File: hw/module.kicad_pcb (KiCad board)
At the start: 2 copper layers, 30 x 30 mm, 35 parts, among them Q1 MUN 2211, U1 CFPS-39, U2 CFPS-39, U3 74LVC1G125, U4 74 LVC 1G3157GW,125, U5 MAX919, U6 STM32L010F4P6, U7 BAS70-7-F, U8 SS39ET, U9 LM 61BIM3

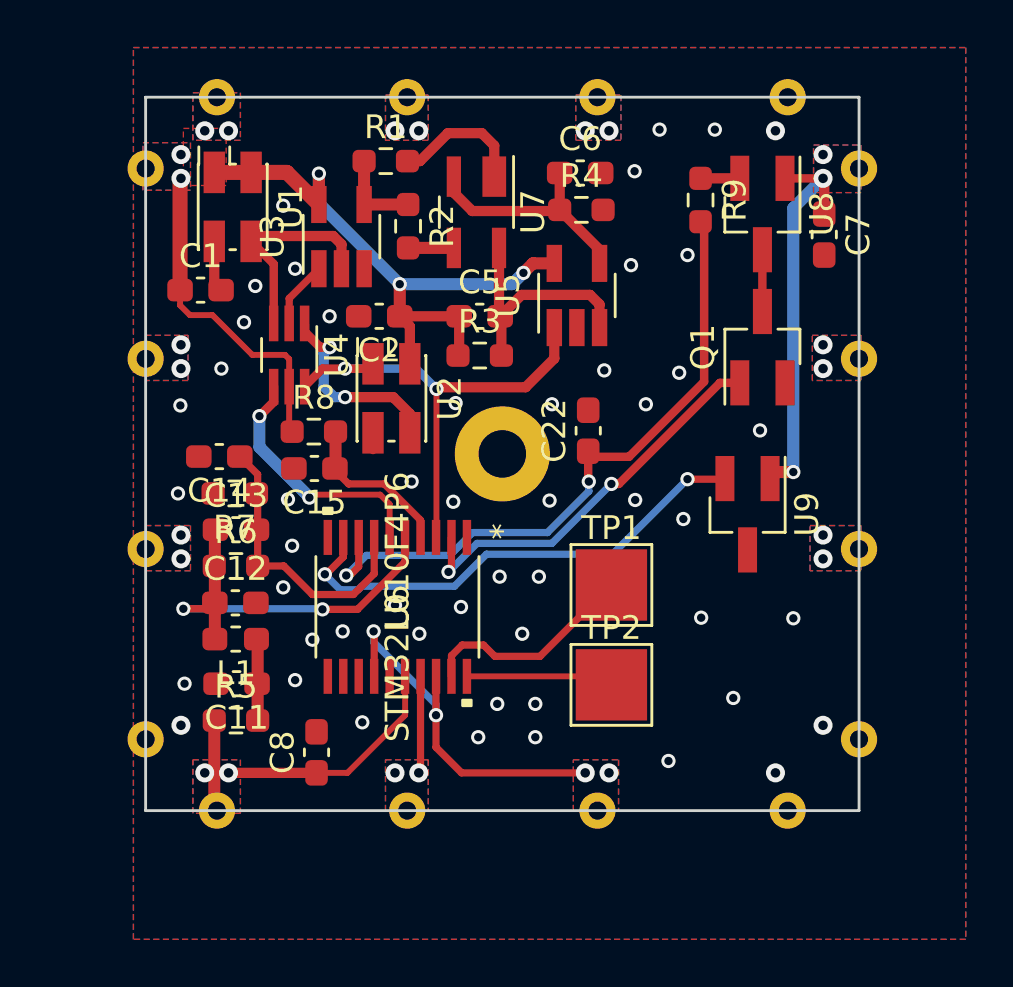
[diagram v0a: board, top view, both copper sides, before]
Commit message: added bom
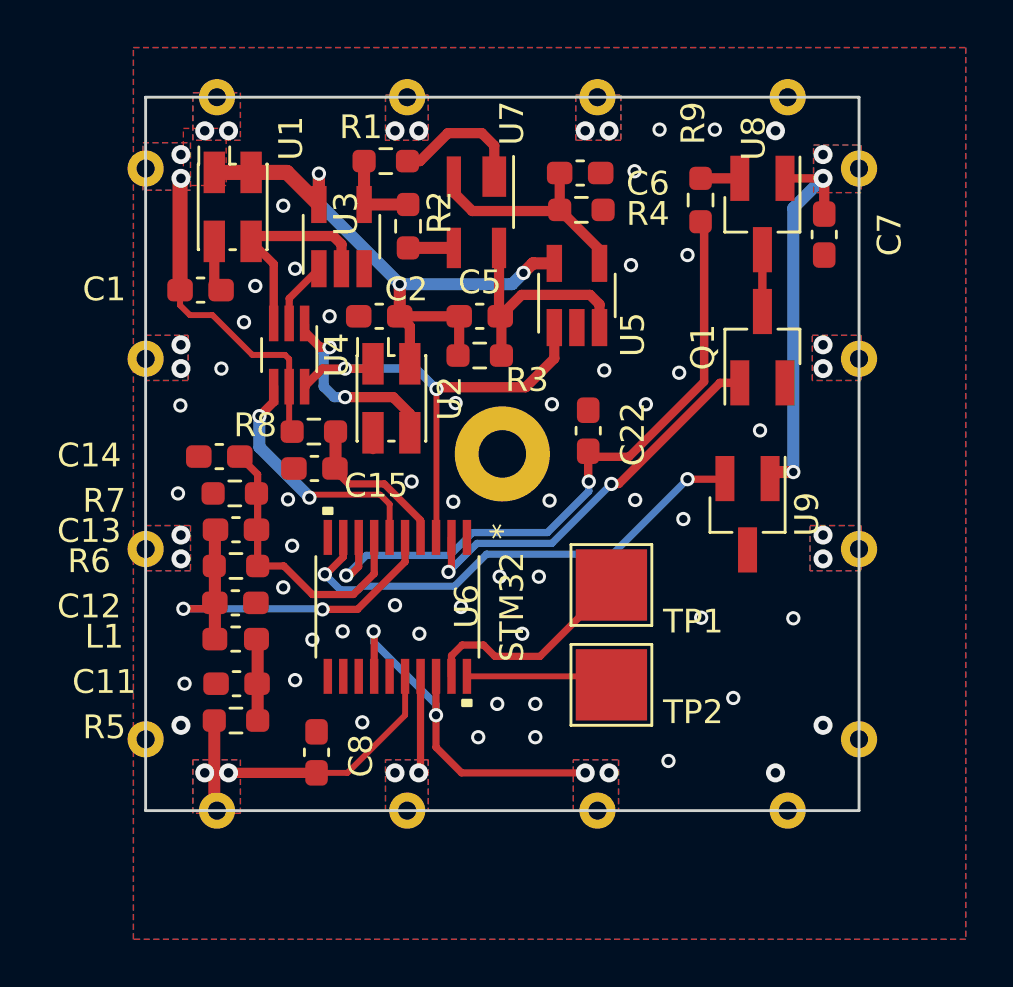
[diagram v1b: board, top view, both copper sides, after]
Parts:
- U6: value STM32L010F4P6 -> STM32
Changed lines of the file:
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@@
     (property "Sheetname" "")
     (attr smd)
-    (fp_text reference "U7" (at -0.02 -2.38 90) (layer "F.SilkS")
+    (fp_text reference "U7" (at -3.745 -1.495 90) (layer "F.SilkS")
       (effects (font (size 1 1) (thickness 0.15)))
     )
@@
     (property "Sheetname" "")
     (attr smd)
-    (fp_text reference "C1" (at 0 -1.43) (layer "F.SilkS")
+    (fp_text reference "C1" (at -4.05 -0.035) (layer "F.SilkS")
       (effects (font (size 1 1) (thickness 0.15)))
     )
@@
     (property "Sheetname" "")
     (attr smd)
-    (fp_text reference "C12" (at 0 -1.43) (layer "F.SilkS")
+    (fp_text reference "C12" (at -6.1475 0.15) (layer "F.SilkS")
       (effects (font (size 1 1) (thickness 0.15)))
     )
@@
     (property "Sheetname" "")
     (attr smd)
-    (fp_text reference "C14" (at 0 -1.43) (layer "F.SilkS")
+    (fp_text reference "C14" (at 5.4725 0.05) (layer "F.SilkS")
       (effects (font (size 1 1) (thickness 0.15)))
     )
@@
     (property "Sheetname" "")
     (attr smd)
-    (fp_text reference "L1" (at 0 -1.43) (layer "F.SilkS")
+    (fp_text reference "L1" (at 5.525 0.105) (layer "F.SilkS")
       (effects (font (size 1 1) (thickness 0.15)))
     )
@@
     (property "Sheetname" "")
     (attr smd)
-    (fp_text reference "U1" (at 0 -2.45 -90) (layer "F.SilkS")
+    (fp_text reference "U1" (at -2.885 -2.45 -90) (layer "F.SilkS")
       (effects (font (size 1 1) (thickness 0.15)))
     )
@@
     (property "Sheetname" "")
     (attr smd)
-    (fp_text reference "C2" (at 0 -1.43 180) (layer "F.SilkS")
+    (fp_text reference "C2" (at -1.1375 1.135 180) (layer "F.SilkS")
       (effects (font (size 1 1) (thickness 0.15)))
     )
@@
     (property "Sheetname" "")
     (attr smd)
-    (fp_text reference "C7" (at 0 -1.43 -90) (layer "F.SilkS")
+    (fp_text reference "C7" (at 0 -2.745 -90) (layer "F.SilkS")
       (effects (font (size 1 1) (thickness 0.15)))
     )
@@
     (property "Sheetname" "")
     (attr smd)
-    (fp_text reference "R4" (at 0 -1.43) (layer "F.SilkS")
+    (fp_text reference "R4" (at 2.7975 0.165) (layer "F.SilkS")
       (effects (font (size 1 1) (thickness 0.15)))
     )
@@
     (property "Sheetname" "")
     (attr smd)
-    (fp_text reference "R2" (at 0 -1.43 -90) (layer "F.SilkS")
+    (fp_text reference "R2" (at -0.5875 -1.315 -90) (layer "F.SilkS")
       (effects (font (size 1 1) (thickness 0.15)))
     )
@@
     (property "Sheetname" "")
     (attr smd)
-    (fp_text reference "R9" (at 0 -1.43 -90) (layer "F.SilkS")
+    (fp_text reference "R9" (at -3.2325 0.31 -90) (layer "F.SilkS")
       (effects (font (size 1 1) (thickness 0.15)))
     )
@@
     (property "Sheetname" "")
     (attr smd)
-    (fp_text reference "U5" (at 0 -2.9 90) (layer "F.SilkS")
+    (fp_text reference "U5" (at -1.645 2.35 90) (layer "F.SilkS")
       (effects (font (size 1 1) (thickness 0.15)))
     )
@@
     (property "Sheetname" "")
     (attr smd)
-    (fp_text reference "C22" (at 0 -1.43 90) (layer "F.SilkS")
+    (fp_text reference "C22" (at -0.146267 1.875 90) (layer "F.SilkS")
       (effects (font (size 1 1) (thickness 0.15)))
     )
@@
     (property "Sheetname" "")
     (attr smd)
-    (fp_text reference "C13" (at 0 -1.43) (layer "F.SilkS")
+    (fp_text reference "C13" (at -6.1725 0.05) (layer "F.SilkS")
       (effects (font (size 1 1) (thickness 0.15)))
     )
@@
     (property "Sheetname" "")
     (attr smd)
-    (fp_text reference "R6" (at 0 -1.43) (layer "F.SilkS")
+    (fp_text reference "R6" (at -6.1725 -0.205) (layer "F.SilkS")
       (effects (font (size 1 1) (thickness 0.15)))
     )
@@
     (property "Sheetname" "")
     (attr smd)
-    (fp_text reference "U8" (at 0 -2.5 90) (layer "F.SilkS")
+    (fp_text reference "U8" (at -3.185 0.37 90) (layer "F.SilkS")
       (effects (font (size 1 1) (thickness 0.15)))
     )
@@
     (property "Sheetname" "")
     (attr smd)
-    (fp_text reference "R8" (at 0 -1.43) (layer "F.SilkS")
+    (fp_text reference "R8" (at -2.4625 -0.27) (layer "F.SilkS")
       (effects (font (size 1 1) (thickness 0.15)))
     )
@@
     (property "Sheetname" "")
     (attr smd)
-    (fp_text reference "R3" (at 0 -1.43) (layer "F.SilkS")
+    (fp_text reference "R3" (at 1.9925 1.025) (layer "F.SilkS")
       (effects (font (size 1 1) (thickness 0.15)))
     )
@@
     (property "Sheetname" "")
     (attr smd)
-    (fp_text reference "C15" (at 0 -1.43) (layer "F.SilkS")
+    (fp_text reference "C15" (at -2.5925 -0.72) (layer "F.SilkS")
       (effects (font (size 1 1) (thickness 0.15)))
     )
@@
     (property "Sheetname" "")
     (attr smd)
-    (fp_text reference "C8" (at 0 -1.43 90) (layer "F.SilkS")
+    (fp_text reference "C8" (at -0.146267 1.87 90) (layer "F.SilkS")
       (effects (font (size 1 1) (thickness 0.15)))
     )
@@
     (property "Sheetname" "")
     (attr exclude_from_pos_files)
-    (fp_text reference "TP2" (at 0 -2.398) (layer "F.SilkS")
+    (fp_text reference "TP2" (at 3.44 1.145) (layer "F.SilkS")
       (effects (font (size 1 1) (thickness 0.15)))
     )
@@
     (property "Sheetname" "")
     (attr smd)
-    (fp_text reference "R1" (at 0 -1.43) (layer "F.SilkS")
+    (fp_text reference "R1" (at -1.0425 -1.43) (layer "F.SilkS")
       (effects (font (size 1 1) (thickness 0.15)))
     )
@@
     (property "Sheetname" "")
     (attr exclude_from_pos_files)
-    (fp_text reference "TP1" (at 0 -2.398) (layer "F.SilkS")
+    (fp_text reference "TP1" (at 3.44 1.535) (layer "F.SilkS")
       (effects (font (size 1 1) (thickness 0.15)))
     )
@@
     (property "Sheetname" "")
     (attr smd)
-    (fp_text reference "U3" (at 0 -2.9 90) (layer "F.SilkS")
+    (fp_text reference "U3" (at 0.96 0.185 90) (layer "F.SilkS")
       (effects (font (size 1 1) (thickness 0.15)))
     )
@@
     (property "Sheetname" "")
     (attr smd)
-    (fp_text reference "R7" (at 0 -1.43) (layer "F.SilkS")
+    (fp_text reference "R7" (at 5.4875 -0.305) (layer "F.SilkS")
       (effects (font (size 1 1) (thickness 0.15)))
     )
@@
     (property "Sheetname" "")
     (attr smd)
-    (fp_text reference "R5" (at 0 -1.43) (layer "F.SilkS")
+    (fp_text reference "R5" (at -5.5375 0.28) (layer "F.SilkS")
       (effects (font (size 1 1) (thickness 0.15)))
     )
@@
     (property "Sheetname" "")
     (attr smd)
-    (fp_text reference "C11" (at 0 -1.43 180) (layer "F.SilkS")
+    (fp_text reference "C11" (at 5.5625 0.075 180) (layer "F.SilkS")
       (effects (font (size 1 1) (thickness 0.15)))
     )
@@
     (property "Sheetname" "")
     (attr through_hole)
-    (fp_text reference "U6" (at 0 0 90) (layer "F.SilkS")
-      (effects (font (size 1 1) (thickness 0.15)))
-    )
-    (fp_text value "STM32L010F4P6" (at 0 0 90) (layer "F.SilkS")
+    (fp_text reference "U6" (at -0.021 -2.915 90) (layer "F.SilkS")
+      (effects (font (size 1 1) (thickness 0.15)))
+    )
+    (fp_text value "STM32" (at 0.000006 -4.82 90) (layer "F.SilkS")
       (effects (font (size 1 1) (thickness 0.15)))
     )
@@
     (property "Sheetname" "")
     (attr smd)
-    (fp_text reference "C6" (at 0 -1.43) (layer "F.SilkS")
-      (effects (font (size 1 1) (thickness 0.15)))
-    )
+    (fp_text reference "C6" (at 2.8475 0.445) (layer "F.SilkS")
+      (effects (font (size 1 1) (thickness 0.15)))
+    )
